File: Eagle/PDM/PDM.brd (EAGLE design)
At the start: 101.3 x 76.2 mm, 43 parts

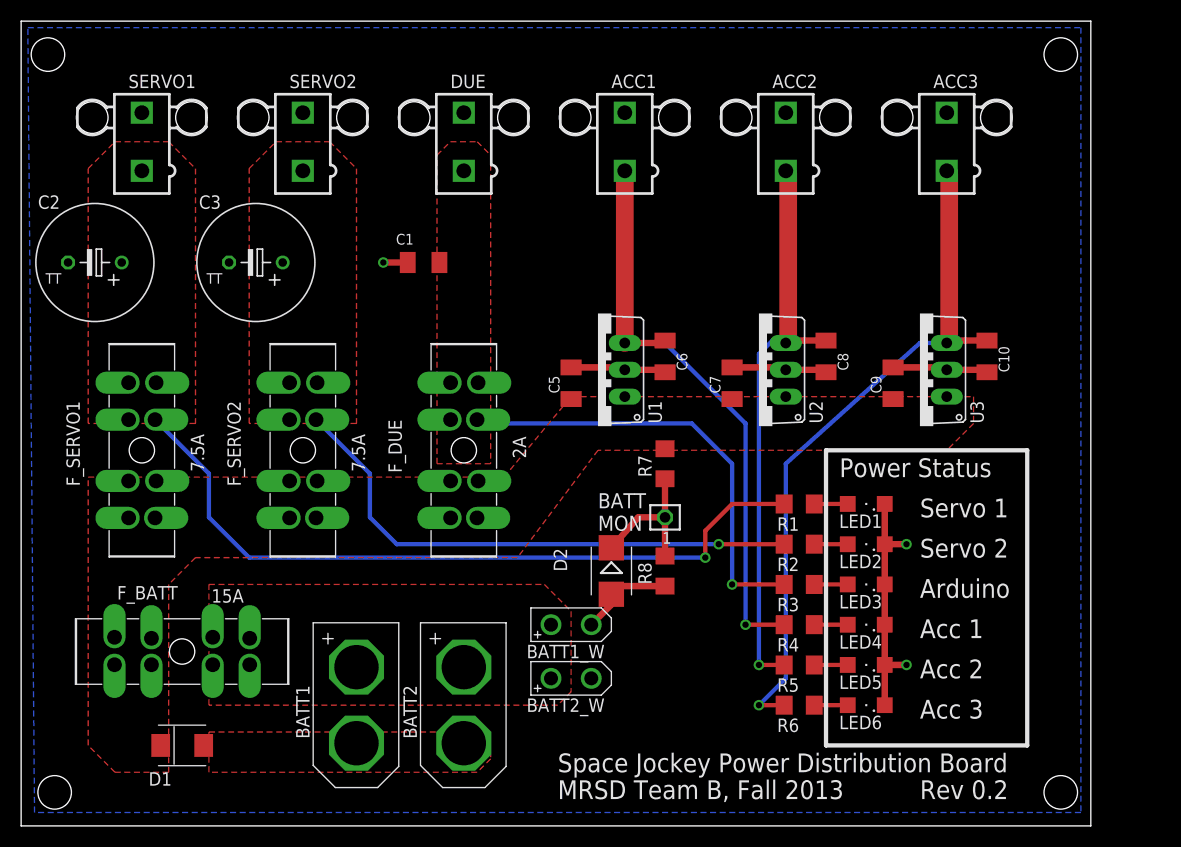
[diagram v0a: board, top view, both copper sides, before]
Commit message: Removed Old PDM, Gerbers added, ready for BOM
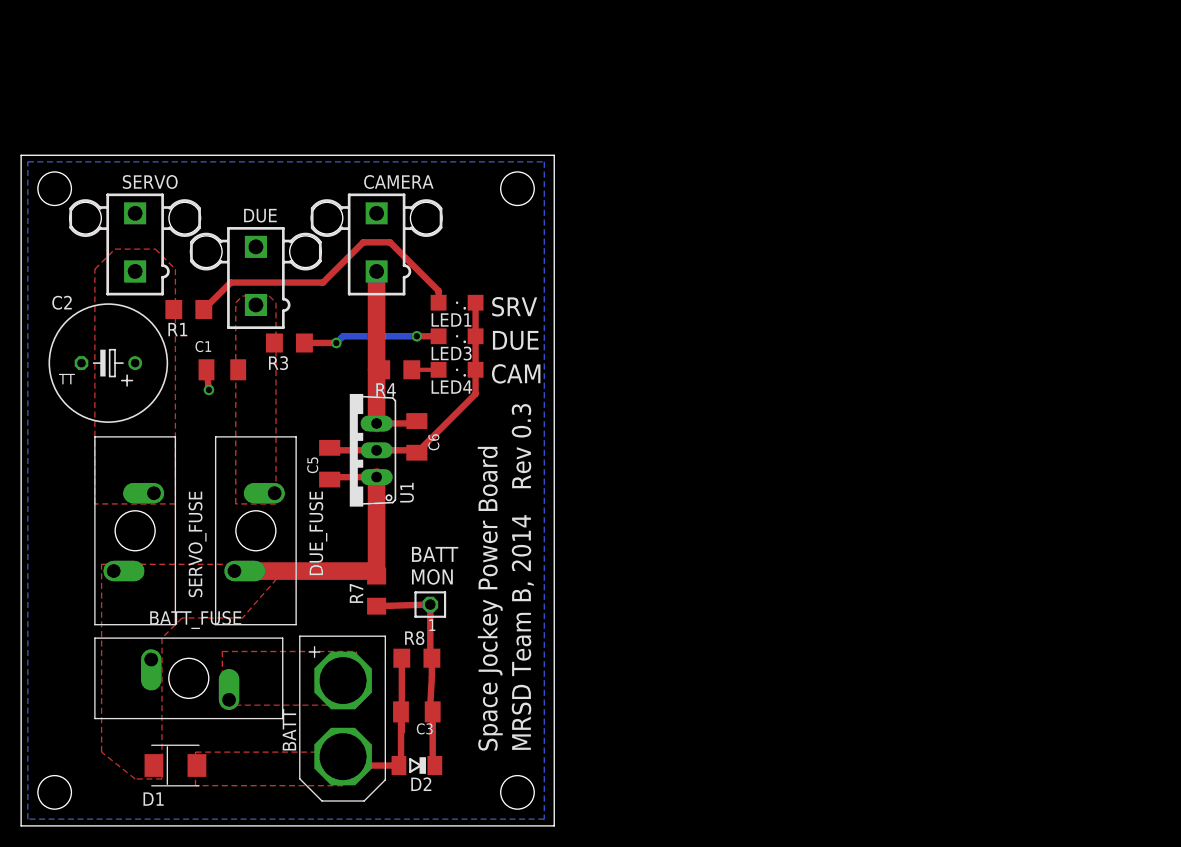
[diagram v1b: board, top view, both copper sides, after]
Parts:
- removed ACC1, ACC2, ACC3, SERVO1, SERVO2: (no value), con-molex:5566-2
- removed BATT1, BATT2: (no value), MRSDTeamB:CON_XT60_PCB_MOUNT
- removed BATT1_W, BATT2_W: (no value), MRSDTeamB:CON_XT60_PIGTAIL
- removed C10, C7, C8, C9: 10uF, rcl:C1206K
- removed F_BATT: 15A, MRSDTeamB:ATO
- removed F_DUE: 2A, MRSDTeamB:ATO
- removed F_SERVO1, F_SERVO2: 7.5A, MRSDTeamB:ATO
- removed LED2, LED5, LED6: (no value), led:SML1206
- removed R2, R5, R6: 1K, rcl:R1206
- removed U2, U3: (no value), MRSDTeamB:TO220V
- added BATT: (no value), MRSDTeamB:CON_XT60_PCB_MALE
- added BATT_FUSE: 10A, MRSDTeamB:MINI_ATO
- added CAMERA, SERVO: (no value), con-molex:5566-2
- added DUE_FUSE: 2A, MRSDTeamB:MINI_ATO
- added SERVO_FUSE: 7.5A, MRSDTeamB:MINI_ATO
- C3: value (none) -> 10uF; device rcl:TT5D11 -> rcl:C1206K
- D2: device diode:SMB -> diode:SOD80C
- R7: value 15.4K -> 1.5K
- R8: value 10K -> 1K
- moved R1 60.6 mm to (15.9, 48.9)
- moved R3 53.4 mm to (25.4, 45.7)
- moved LED4 45.6 mm to (41.3, 43.2)
- moved LED3 45.3 mm to (41.3, 46.4)
- moved C3 45.2 mm to (37.5, 10.8)
- moved R4 45.1 mm to (35.6, 43.2)
- moved LED1 43.2 mm to (41.3, 49.5)
- moved R7 29.9 mm to (33.7, 22.2)
- moved D2 26.0 mm to (37.5, 5.71), turned to 180 degrees
- moved R8 24.9 mm to (37.5, 15.9), turned to 0 degrees
- moved C6 24.7 mm to (37.5, 36.8)
- moved U1 24.7 mm to (31.1, 35.6)
- moved C5 24.1 mm to (29.2, 34.3)
- moved BAT_MON 23.7 mm to (38.7, 21.0)
- moved DUE 23.4 mm to (22.2, 52.1)
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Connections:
- removed net N$1: C3.+, F_SERVO2.B1, F_SERVO2.B2, F_SERVO2.B3, F_SERVO2.B4, R2.2, SERVO2.1
- removed net N$16: LED5.A, R5.1
- removed net N$19: ACC3.1, C10.1, R6.2, U3.3
- removed net N$22: LED6.A, R6.1
- removed net N$8: LED2.A, R2.1
- removed net N$9: ACC2.1, C8.1, R5.2, U2.3
- net GND: now also BATT.V-, C3.2, CAMERA.2, SERVO.2; no longer ACC1.2, ACC2.2, ACC3.2, BATT1.V-, BATT1_W.V-, BATT2.V-, BATT2_W.V-, C10.2, C3.-, C7.2, C8.2, C9.2, LED2.C, LED5.C, LED6.C, SERVO1.2, SERVO2.2, U2.2, U3.2
- net N$15: now also SERVO.1, SERVO_FUSE.P$3; no longer F_SERVO1.B1, F_SERVO1.B2, F_SERVO1.B3, F_SERVO1.B4, SERVO1.1
- net N$18: now also C3.1
- net N$2: now also BATT.V+, BATT_FUSE.P$2; no longer BATT1.V+, BATT1_W.V+, BATT2.V+, BATT2_W.V+, F_BATT.A1, F_BATT.A2, F_BATT.A3, F_BATT.A4
- net N$4: now also DUE_FUSE.P$3; no longer F_DUE.B1, F_DUE.B2, F_DUE.B3, F_DUE.B4
- net N$6: now also CAMERA.1; no longer ACC1.1
- net V_SUPPLY: now also BATT_FUSE.P$3, DUE_FUSE.P$2, SERVO_FUSE.P$2; no longer C7.1, C9.1, F_BATT.B1, F_BATT.B2, F_BATT.B3, F_BATT.B4, F_DUE.A1, F_DUE.A2, F_DUE.A3, F_DUE.A4, F_SERVO1.A1, F_SERVO1.A2, F_SERVO1.A3, F_SERVO1.A4, F_SERVO2.A1, F_SERVO2.A2, F_SERVO2.A3, F_SERVO2.A4, U2.1, U3.1
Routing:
- net N$15: track 71.0 -> 0.00 mm, vias 1 -> 0
- net N$19: track 66.0 -> 0.00 mm, vias 1 -> 0
- net N$9: track 55.5 -> 0.00 mm, vias 1 -> 0
- net N$1: track 51.6 -> 0.00 mm, vias 1 -> 0
- net N$4: track 42.2 -> 0.00 mm, vias 1 -> 0
- net N$6: track 57.6 -> 18.8 mm, vias 1 -> 0
- net V_SUPPLY: track 0.00 -> 26.8 mm
- net N$5: track 3.18 -> 27.9 mm
- net GND: track 62.3 -> 46.8 mm, vias 3 -> 1
- net N$11: track 3.18 -> 13.0 mm, vias 0 -> 2
- net N$18: track 13.7 -> 21.0 mm
- net N$8: track 3.18 -> 0.00 mm
- net N$22: track 3.18 -> 0.00 mm
- net N$16: track 3.18 -> 0.00 mm
- net N$13: track 3.18 -> 2.54 mm
- removed copper zone on layer 1, net N$1
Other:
- board size 101.3 x 76.2 mm -> 50.5 x 63.5 mm
- board text added: "CAM"
- board text added: "DUE"
- board text added: "MRSD Team B, 2014"
- board text added: "Rev 0.3"
- board text added: "SRV"
- board text added: "Space Jockey Power Board"
- board text removed: "Acc 1"
- board text removed: "Acc 2"
- board text removed: "Acc 3"
- board text removed: "Arduino"
- board text removed: "MRSD Team B, Fall 2013"
- board text removed: "Power Status"
- board text removed: "Rev 0.2"
- board text removed: "Servo 1"
- board text removed: "Servo 2"
- board text removed: "Space Jockey Power Distribution Board"
